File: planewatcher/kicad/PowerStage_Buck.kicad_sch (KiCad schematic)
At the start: 19 parts, among them U11 LT8640IUDCF-1#PBF

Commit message: work on board layout
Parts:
- renumbered C104 to C59, C105 to C60, C60 to C61, C61 to C62, C62 to C63, C63 to C64, C64 to C66, C66 to C67, L7 to L10, L14 to L9, R56 to R32, R26 to R33, R27 to R34, R28 to R35, TP16 to TP18, TP15 to TP19, U11 to U12
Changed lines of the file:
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@@
 		(in_pos_files yes)
 		(dnp no)
-		(property "Reference" "#PWR089"
+		(property "Reference" "#PWR097"
 			(at 161.29 81.28 0)
 			(hide yes)
@@
 			(project "planewatcher"
 				(path "/7a4a4324-e8b8-4d06-b75a-28095d4e9f10/3f548880-1f88-4cb2-a308-e70fd70c9481"
-					(reference "#PWR089")
+					(reference "#PWR097")
 					(unit 1)
 				)
@@
 		(dnp no)
 		(fields_autoplaced yes)
-		(property "Reference" "L14"
+		(property "Reference" "L9"
 			(at 99.06 54.61 90)
 			(show_name no)
@@
 			(project "planewatcher"
 				(path "/7a4a4324-e8b8-4d06-b75a-28095d4e9f10/3f548880-1f88-4cb2-a308-e70fd70c9481"
-					(reference "L14")
+					(reference "L9")
 					(unit 1)
 				)
@@
 		(dnp no)
 		(fields_autoplaced yes)
-		(property "Reference" "#PWR035"
+		(property "Reference" "#PWR099"
 			(at 119.38 107.95 0)
 			(hide yes)
@@
 			(project "planewatcher"
 				(path "/7a4a4324-e8b8-4d06-b75a-28095d4e9f10/3f548880-1f88-4cb2-a308-e70fd70c9481"
-					(reference "#PWR035")
+					(reference "#PWR099")
 					(unit 1)
 				)
@@
 		(in_pos_files yes)
 		(dnp no)
-		(property "Reference" "C63"
+		(property "Reference" "C64"
 			(at 115.57 87.63 90)
 			(show_name no)
@@
 			(project "planewatcher"
 				(path "/7a4a4324-e8b8-4d06-b75a-28095d4e9f10/3f548880-1f88-4cb2-a308-e70fd70c9481"
-					(reference "C63")
+					(reference "C64")
 					(unit 1)
 				)
@@
 		(dnp no)
 		(fields_autoplaced yes)
-		(property "Reference" "U11"
+		(property "Reference" "U12"
 			(at 143.51 110.49 0)
 			(show_name no)
@@
 			(project "planewatcher"
 				(path "/7a4a4324-e8b8-4d06-b75a-28095d4e9f10/3f548880-1f88-4cb2-a308-e70fd70c9481"
-					(reference "U11")
+					(reference "U12")
 					(unit 1)
 				)
@@
 		(in_pos_files yes)
 		(dnp no)
-		(property "Reference" "R28"
+		(property "Reference" "R35"
 			(at 119.38 117.348 90)
 			(show_name no)
@@
 			(project "planewatcher"
 				(path "/7a4a4324-e8b8-4d06-b75a-28095d4e9f10/3f548880-1f88-4cb2-a308-e70fd70c9481"
-					(reference "R28")
+					(reference "R35")
 					(unit 1)
 				)
@@
 		(dnp no)
 		(fields_autoplaced yes)
-		(property "Reference" "L7"
+		(property "Reference" "L10"
 			(at 180.34 85.09 90)
 			(show_name no)
@@
 			(project "planewatcher"
 				(path "/7a4a4324-e8b8-4d06-b75a-28095d4e9f10/3f548880-1f88-4cb2-a308-e70fd70c9481"
-					(reference "L7")
+					(reference "L10")
 					(unit 1)
 				)
@@
 		(dnp no)
 		(fields_autoplaced yes)
-		(property "Reference" "#PWR041"
+		(property "Reference" "#PWR0101"
 			(at 156.21 111.76 0)
 			(hide yes)
@@
 			(project "planewatcher"
 				(path "/7a4a4324-e8b8-4d06-b75a-28095d4e9f10/3f548880-1f88-4cb2-a308-e70fd70c9481"
-					(reference "#PWR041")
+					(reference "#PWR0101")
 					(unit 1)
 				)
@@
 		(dnp no)
 		(fields_autoplaced yes)
-		(property "Reference" "R26"
+		(property "Reference" "R33"
 			(at 193.04 96.5199 0)
 			(show_name no)
@@
 			(project "planewatcher"
 				(path "/7a4a4324-e8b8-4d06-b75a-28095d4e9f10/3f548880-1f88-4cb2-a308-e70fd70c9481"
-					(reference "R26")
+					(reference "R33")
 					(unit 1)
 				)
@@
 		(in_pos_files yes)
 		(dnp no)
-		(property "Reference" "C66"
+		(property "Reference" "C67"
 			(at 122.936 95.758 90)
 			(show_name no)
@@
 			(project "planewatcher"
 				(path "/7a4a4324-e8b8-4d06-b75a-28095d4e9f10/3f548880-1f88-4cb2-a308-e70fd70c9481"
-					(reference "C66")
+					(reference "C67")
 					(unit 1)
 				)
@@
 		(dnp no)
 		(fields_autoplaced yes)
-		(property "Reference" "C104"
+		(property "Reference" "C59"
 			(at 95.25 62.2299 0)
 			(show_name no)
@@
 			(project "planewatcher"
 				(path "/7a4a4324-e8b8-4d06-b75a-28095d4e9f10/3f548880-1f88-4cb2-a308-e70fd70c9481"
-					(reference "C104")
+					(reference "C59")
 					(unit 1)
 				)
@@
 		(in_pos_files yes)
 		(dnp no)
-		(property "Reference" "TP15"
+		(property "Reference" "TP19"
 			(at 85.344 96.012 90)
 			(show_name no)
@@
 			(project "planewatcher"
 				(path "/7a4a4324-e8b8-4d06-b75a-28095d4e9f10/3f548880-1f88-4cb2-a308-e70fd70c9481"
-					(reference "TP15")
+					(reference "TP19")
 					(unit 1)
 				)
@@
 		(in_pos_files yes)
 		(dnp no)
-		(property "Reference" "C62"
+		(property "Reference" "C63"
 			(at 164.592 85.344 0)
 			(show_name no)
@@
 			(project "planewatcher"
 				(path "/7a4a4324-e8b8-4d06-b75a-28095d4e9f10/3f548880-1f88-4cb2-a308-e70fd70c9481"
-					(reference "C62")
+					(reference "C63")
 					(unit 1)
 				)
@@
 		(dnp no)
 		(fields_autoplaced yes)
-		(property "Reference" "C60"
+		(property "Reference" "C61"
 			(at 125.73 69.8499 0)
 			(show_name no)
@@
 			(project "planewatcher"
 				(path "/7a4a4324-e8b8-4d06-b75a-28095d4e9f10/3f548880-1f88-4cb2-a308-e70fd70c9481"
-					(reference "C60")
+					(reference "C61")
 					(unit 1)
 				)
@@
 		(dnp no)
 		(fields_autoplaced yes)
-		(property "Reference" "#PWR088"
+		(property "Reference" "#PWR096"
 			(at 121.92 81.28 0)
 			(hide yes)
@@
 			(project "planewatcher"
 				(path "/7a4a4324-e8b8-4d06-b75a-28095d4e9f10/3f548880-1f88-4cb2-a308-e70fd70c9481"
-					(reference "#PWR088")
+					(reference "#PWR096")
 					(unit 1)
 				)
@@
 		(dnp no)
 		(fields_autoplaced yes)
-		(property "Reference" "R56"
+		(property "Reference" "R32"
 			(at 92.71 88.9 90)
 			(show_name no)
@@
 			(project "planewatcher"
 				(path "/7a4a4324-e8b8-4d06-b75a-28095d4e9f10/3f548880-1f88-4cb2-a308-e70fd70c9481"
-					(reference "R56")
+					(reference "R32")
 					(unit 1)
 				)
@@
 		(dnp no)
 		(fields_autoplaced yes)
-		(property "Reference" "#PWR091"
+		(property "Reference" "#PWR0100"
 			(at 204.47 107.95 0)
 			(hide yes)
@@
 			(project "planewatcher"
 				(path "/7a4a4324-e8b8-4d06-b75a-28095d4e9f10/3f548880-1f88-4cb2-a308-e70fd70c9481"
-					(reference "#PWR091")
+					(reference "#PWR0100")
 					(unit 1)
 				)
@@
 		(dnp no)
 		(fields_autoplaced yes)
-		(property "Reference" "#PWR092"
+		(property "Reference" "#PWR0102"
 			(at 190.5 115.57 0)
 			(hide yes)
@@
 			(project "planewatcher"
 				(path "/7a4a4324-e8b8-4d06-b75a-28095d4e9f10/3f548880-1f88-4cb2-a308-e70fd70c9481"
-					(reference "#PWR092")
+					(reference "#PWR0102")
 					(unit 1)
 				)
@@
 		(dnp no)
 		(fields_autoplaced yes)
-		(property "Reference" "#PWR040"
+		(property "Reference" "#PWR0103"
 			(at 114.3 128.27 0)
 			(hide yes)
@@
 			(project "planewatcher"
 				(path "/7a4a4324-e8b8-4d06-b75a-28095d4e9f10/3f548880-1f88-4cb2-a308-e70fd70c9481"
-					(reference "#PWR040")
+					(reference "#PWR0103")
 					(unit 1)
 				)
@@
 		(dnp no)
 		(fields_autoplaced yes)
-		(property "Reference" "#PWR0148"
+		(property "Reference" "#PWR095"
 			(at 106.68 73.66 0)
 			(hide yes)
@@
 			(project "planewatcher"
 				(path "/7a4a4324-e8b8-4d06-b75a-28095d4e9f10/3f548880-1f88-4cb2-a308-e70fd70c9481"
-					(reference "#PWR0148")
+					(reference "#PWR095")
 					(unit 1)
 				)
@@
 		(in_pos_files yes)
 		(dnp no)
-		(property "Reference" "TP16"
+		(property "Reference" "TP18"
 			(at 189.738 82.296 0)
 			(show_name no)
@@
 			(project "planewatcher"
 				(path "/7a4a4324-e8b8-4d06-b75a-28095d4e9f10/3f548880-1f88-4cb2-a308-e70fd70c9481"
-					(reference "TP16")
+					(reference "TP18")
 					(unit 1)
 				)
@@
 		(dnp no)
 		(fields_autoplaced yes)
-		(property "Reference" "#PWR034"
+		(property "Reference" "#PWR098"
 			(at 111.76 100.33 0)
 			(hide yes)
@@
 			(project "planewatcher"
 				(path "/7a4a4324-e8b8-4d06-b75a-28095d4e9f10/3f548880-1f88-4cb2-a308-e70fd70c9481"
-					(reference "#PWR034")
+					(reference "#PWR098")
 					(unit 1)
 				)
@@
 		(dnp no)
 		(fields_autoplaced yes)
-		(property "Reference" "#PWR0132"
+		(property "Reference" "#PWR094"
 			(at 91.44 73.66 0)
 			(hide yes)
@@
 			(project "planewatcher"
 				(path "/7a4a4324-e8b8-4d06-b75a-28095d4e9f10/3f548880-1f88-4cb2-a308-e70fd70c9481"
-					(reference "#PWR0132")
+					(reference "#PWR094")
 					(unit 1)
 				)
@@
 		(dnp no)
 		(fields_autoplaced yes)
-		(property "Reference" "C105"
+		(property "Reference" "C60"
 			(at 110.49 62.2299 0)
 			(show_name no)
@@
 			(project "planewatcher"
 				(path "/7a4a4324-e8b8-4d06-b75a-28095d4e9f10/3f548880-1f88-4cb2-a308-e70fd70c9481"
-					(reference "C105")
+					(reference "C60")
 					(unit 1)
 				)
@@
 		(dnp no)
 		(fields_autoplaced yes)
-		(property "Reference" "R27"
+		(property "Reference" "R34"
 			(at 193.04 104.1399 0)
 			(show_name no)
@@
 			(project "planewatcher"
 				(path "/7a4a4324-e8b8-4d06-b75a-28095d4e9f10/3f548880-1f88-4cb2-a308-e70fd70c9481"
-					(reference "R27")
+					(reference "R34")
 					(unit 1)
 				)
@@
 		(dnp no)
 		(fields_autoplaced yes)
-		(property "Reference" "C61"
+		(property "Reference" "C62"
 			(at 165.1 69.8499 0)
 			(show_name no)
@@
 			(project "planewatcher"
 				(path "/7a4a4324-e8b8-4d06-b75a-28095d4e9f10/3f548880-1f88-4cb2-a308-e70fd70c9481"
-					(reference "C61")
+					(reference "C62")
 					(unit 1)
 				)
@@
 		(dnp no)
 		(fields_autoplaced yes)
-		(property "Reference" "C64"
+		(property "Reference" "C66"
 			(at 208.28 96.5199 0)
 			(show_name no)
@@
 			(project "planewatcher"
 				(path "/7a4a4324-e8b8-4d06-b75a-28095d4e9f10/3f548880-1f88-4cb2-a308-e70fd70c9481"
-					(reference "C64")
-					(unit 1)
-				)
+					(reference "C66")
+					(unit 1)
+				)

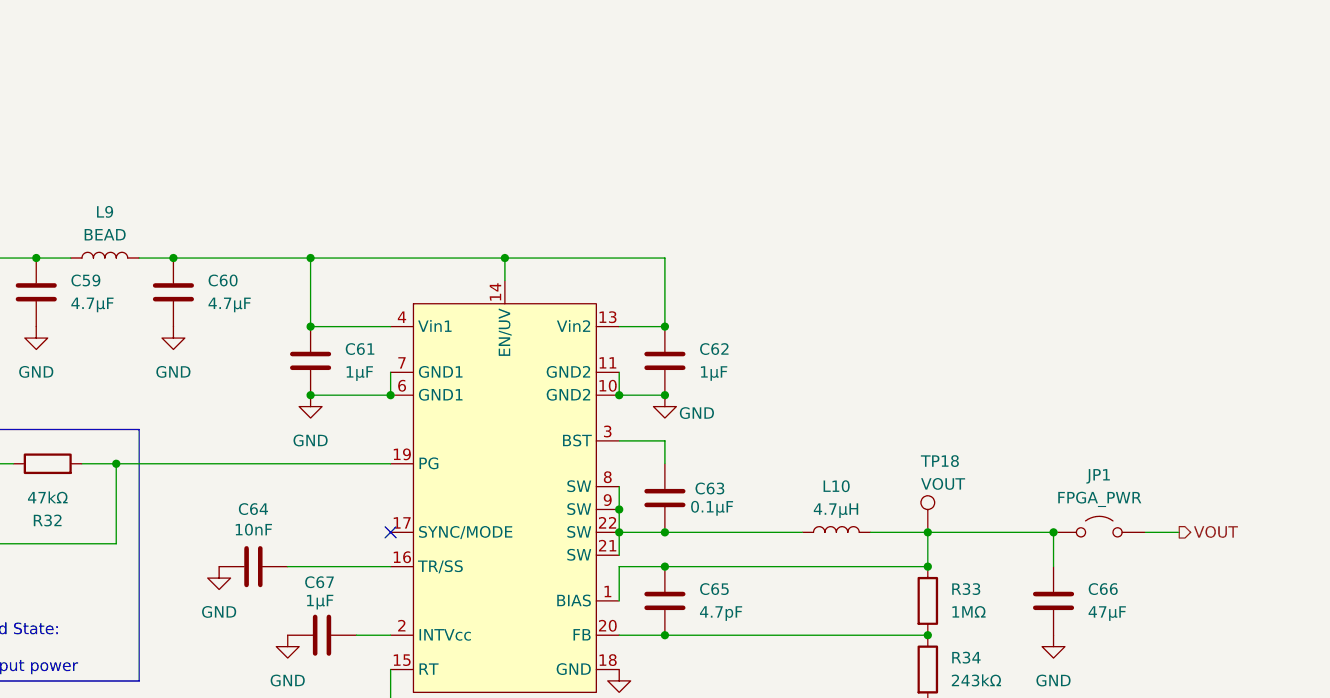
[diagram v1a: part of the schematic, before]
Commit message: address & fix ERC errors/warnings
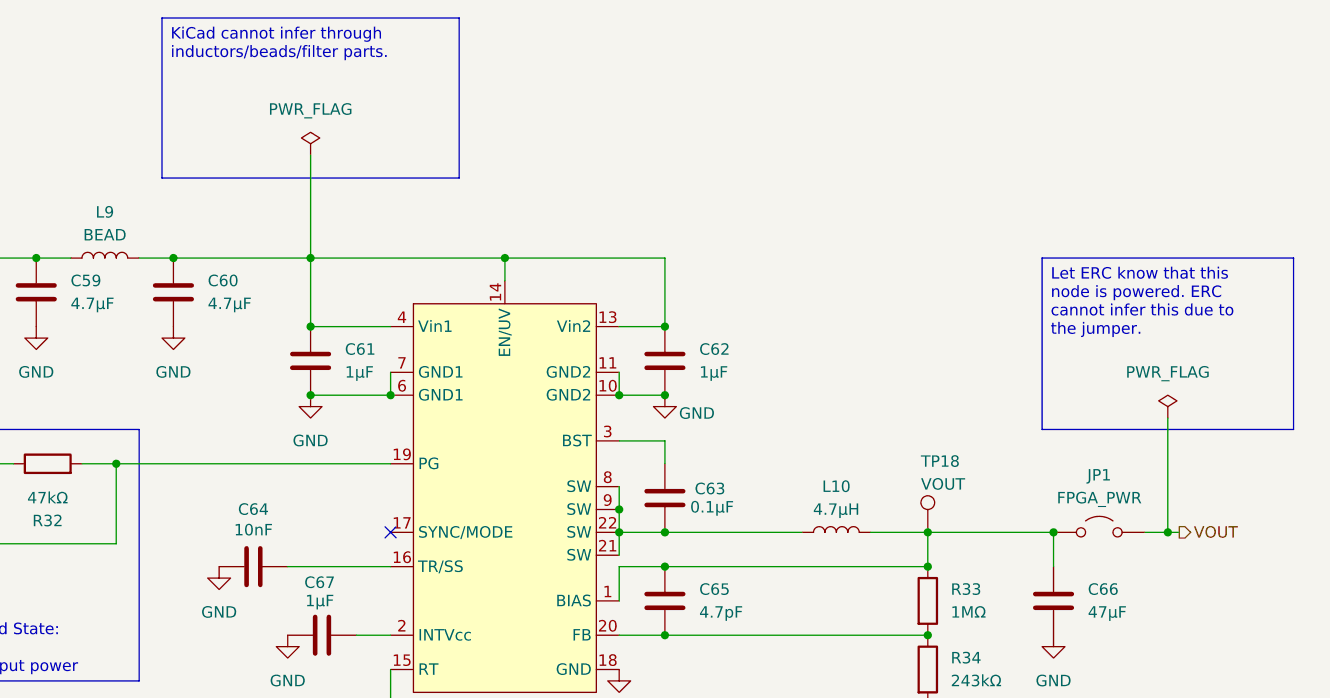
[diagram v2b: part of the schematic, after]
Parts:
- JP1: Notes (none) -> Allow FPGA power to be disconnected, if FPGA powered extern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
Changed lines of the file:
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@@
 		)
 	)
+	(text_box "Let ERC know that this node is powered. ERC cannot infer this due to the jumper."
+		(exclude_from_sim no)
+		(at 203.2 59.69 0)
+		(size 27.94 19.05)
+		(margins 0.9525 0.9525 0.9525 0.9525)
+		(stroke
+			(width 0)
+			(type solid)
+		)
+		(fill
+			(type none)
+		)
+		(effects
+			(font
+				(size 1.27 1.27)
+			)
+			(justify left top)
+		)
+	)
 	(text_box "Set switching freq. to 700kHz."
 		(exclude_from_sim no)
@@
 		)
 	)
+	(text_box "KiCad cannot infer through inductors/beads/filter parts."
+		(exclude_from_sim no)
+		(at 105.41 33.02 0)
+		(size 33.02 17.78)
+		(margins 0.9525 0.9525 0.9525 0.9525)
+		(stroke
+			(width 0)
+			(type solid)
+		)
+		(fill
+			(type none)
+		)
+		(effects
+			(font
+				(size 1.27 1.27)
+			)
+			(justify left top)
+		)
+	)
 	(junction
 		(at 190.5 93.98)
@@
 	)
 	(junction
+		(at 217.17 90.17)
+		(diameter 0)
+		(color 0 0 0 0)
+	)
+	(junction
 		(at 156.21 90.17)
 		(diameter 0)
@@
 	(wire
 		(pts
+			(xy 121.92 48.26) (xy 121.92 59.69)
+		)
+		(stroke
+			(width 0)
+			(type default)
+		)
+	)
+	(wire
+		(pts
 			(xy 119.38 93.98) (xy 130.81 93.98)
 		)
@@
 	(wire
 		(pts
+			(xy 217.17 77.47) (xy 217.17 90.17)
+		)
+		(stroke
+			(width 0)
+			(type default)
+		)
+	)
+	(wire
+		(pts
 			(xy 156.21 85.09) (xy 156.21 87.63)
 		)
@@
 	(wire
 		(pts
-			(xy 214.63 90.17) (xy 218.44 90.17)
+			(xy 214.63 90.17) (xy 217.17 90.17)
 		)
 		(stroke
@@
 	(wire
 		(pts
+			(xy 217.17 90.17) (xy 218.44 90.17)
+		)
+		(stroke
+			(width 0)
+			(type default)
+		)
+	)
+	(wire
+		(pts
 			(xy 121.92 74.93) (xy 130.81 74.93)
 		)
@@
 	)
 	(symbol
+		(lib_id "power:PWR_FLAG")
+		(at 217.17 77.47 0)
+		(unit 1)
+		(body_style 1)
+		(exclude_from_sim no)
+		(in_bom yes)
+		(on_board yes)
+		(in_pos_files yes)
+		(dnp no)
+		(fields_autoplaced yes)
+		(property "Reference" "#FLG01"
+			(at 217.17 75.565 0)
+			(hide yes)
+			(show_name no)
+			(do_not_autoplace no)
+			(effects
+				(font
+					(size 1.27 1.27)
+				)
+			)
+		)
+		(property "Value" "PWR_FLAG"
+			(at 217.17 72.39 0)
+			(show_name no)
+			(do_not_autoplace no)
+			(effects
+				(font
+					(size 1.27 1.27)
+				)
+			)
+		)
+		(property "Footprint" ""
+			(at 217.17 77.47 0)
+			(hide yes)
+			(show_name no)
+			(do_not_autoplace no)
+			(effects
+				(font
+					(size 1.27 1.27)
+				)
+			)
+		)
+		(property "Datasheet" ""
+			(at 217.17 77.47 0)
+			(hide yes)
+			(show_name no)
+			(do_not_autoplace no)
+			(effects
+				(font
+					(size 1.27 1.27)
+				)
+			)
+		)
+		(property "Description" "Special symbol for telling ERC where power comes from"
+			(at 217.17 77.47 0)
+			(hide yes)
+			(show_name no)
+			(do_not_autoplace no)
+			(effects
+				(font
+					(size 1.27 1.27)
+				)
+			)
+		)
+		(pin "1"
+		)
+		(instances
+			(project "planewatcher"
+				(path "/7a4a4324-e8b8-4d06-b75a-28095d4e9f10/3f548880-1f88-4cb2-a308-e70fd70c9481"
+					(reference "#FLG01")
+					(unit 1)
+				)
+			)
+		)
+	)
+	(symbol
 		(lib_id "power:GND")
 		(at 121.92 74.93 0)
@@
 			)
 		)
-		(property "Notes" ""
+		(property "Notes" "Allow FPGA power to be disconnected, if FPGA powered externally."
 			(at 209.55 90.17 0)
 			(hide yes)
@@
 					(unit 1)
 				)
+			)
+		)
+	)
+	(symbol
+		(lib_id "power:PWR_FLAG")
+		(at 121.92 48.26 0)
+		(unit 1)
+		(body_style 1)
+		(exclude_from_sim no)
+		(in_bom yes)
+		(on_board yes)
+		(in_pos_files yes)
+		(dnp no)
+		(fields_autoplaced yes)
+		(property "Reference" "#FLG010"
+			(at 121.92 46.355 0)
+			(hide yes)
+			(show_name no)
+			(do_not_autoplace no)
+			(effects
+				(font
+					(size 1.27 1.27)
+				)
+			)
+		)
+		(property "Value" "PWR_FLAG"
+			(at 121.92 43.18 0)
+			(show_name no)
+			(do_not_autoplace no)
+			(effects
+				(font
+					(size 1.27 1.27)
+				)
+			)
+		)
+		(property "Footprint" ""
+			(at 121.92 48.26 0)
+			(hide yes)
+			(show_name no)
+			(do_not_autoplace no)
+			(effects
+				(font
+					(size 1.27 1.27)
+				)
+			)
+		)
+		(property "Datasheet" ""
+			(at 121.92 48.26 0)
+			(hide yes)
+			(show_name no)
+			(do_not_autoplace no)
+			(effects
+				(font
+					(size 1.27 1.27)
+				)
+			)
+		)
+		(property "Description" "Special symbol for telling ERC where power comes from"
+			(at 121.92 48.26 0)
+			(hide yes)
+			(show_name no)
+			(do_not_autoplace no)
+			(effects
+				(font
+					(size 1.27 1.27)
+				)
+			)
+		)
+		(pin "1"
+		)
+		(instances
+			(project "planewatcher"
+				(path "/7a4a4324-e8b8-4d06-b75a-28095d4e9f10/3f548880-1f88-4cb2-a308-e70fd70c9481"
+					(reference "#FLG010")
+					(unit 1)
+				)

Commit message: updates before fab
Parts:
- C59, C60: Purpose (none) -> Input ceramic capacitor for the LT8640 buck regulator.; Suggested Part (none) -> Murata GRM31CR71E475KA88L
- C61, C62: Purpose (none) -> Local 1µF VIN bypass capacitor for the LT8640 buck regulato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; Suggested Part (none) -> Murata GRM188R61C105KA93D
- C63: Purpose (none) -> LT8640 BST-to-SW bootstrap capacitor for the high-side swit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; Suggested Part (none) -> Murata GRM155R71H104KE14D
- C64: Purpose (none) -> Soft-start or regulator control bypass capacitor in the LT8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; Suggested Part (none) -> Murata GRM155R71H103KA88D
- C65: Purpose (none) -> Feed-forward/compensation capacitor across the LT8640 feedb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; Suggested Part (none) -> Murata GRM1555C1H4R7CA01D
- C66: Purpose (none) -> LT8640 output bulk capacitor for FPGA rail ripple and load 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; Suggested Part (none) -> KEMET C1210C476M4PACTU
- C67: Purpose (none) -> Regulator auxiliary/input bypass capacitor in the LT8640 bu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; Suggested Part (none) -> Murata GRM155R61C105KA12D
- JP1: Purpose (none) -> Allows the FPGA power rail to be linked or isolated during 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; Suggested Part (none) -> Samtec TSW-102-07-L-S
- L10: Purpose (none) -> LT8640 buck switching inductor for the FPGA 5V supply.; Suggested Part (none) -> Coilcraft XAL5030-472ME
- L9: Purpose (none) -> Filters high-frequency switching noise on the LT8640 regula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; Suggested Part (none) -> Murata BLM21PG600SN1D
- R32: Purpose (none) -> LT8640 power-good pull-up or regulator status bias resistor.; Suggested Part (none) -> Yageo RC0402FR-0747KL
- R33: Purpose (none) -> Top feedback resistor setting the LT8640 FPGA 5V output vol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; Suggested Part (none) -> Yageo RC0402FR-071ML
- R34: Purpose (none) -> Bottom/trim feedback resistor setting the LT8640 output vol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; Suggested Part (none) -> Yageo RC0402FR-07243KL
- R35: Purpose (none) -> LT8640 RT resistor setting the FPGA buck switching frequenc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; Suggested Part (none) -> Yageo RC0402FR-0760K4L
- TP18: Purpose (none) -> Provides oscilloscope/DMM probe access to VOUT.; Suggested Part (none) -> No fitted part (PCB pad only); now left out of the parts list
- TP19: Purpose (none) -> Provides oscilloscope/DMM probe access to PG.; Suggested Part (none) -> No fitted part (PCB pad only); now left out of the parts list
- U12: Purpose (none) -> Generates the FPGA 5V rail from the protected input supply.; Suggested Part (none) -> Analog Devices LT8640IUDCF-1#PBF

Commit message: updates before fab
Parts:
- JP1: now not fitted
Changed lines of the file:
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@@
 		(on_board yes)
 		(in_pos_files yes)
-		(dnp no)
+		(dnp yes)
 		(fields_autoplaced yes)
 		(property "Reference" "JP1"

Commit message: rationalise power to single 3V3 rail fed from FPGA VCC
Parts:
- U12: now not fitted
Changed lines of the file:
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@@
 		(on_board yes)
 		(in_pos_files yes)
-		(dnp no)
+		(dnp yes)
 		(fields_autoplaced yes)
 		(property "Reference" "U12"

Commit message: Add persistent PCBWay BOM fields to KiCad schematic
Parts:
- C59, C60: MPN (none) -> GRM31CR71E475KA88L; Manufacturer (none) -> Murata; Package (none) -> 1206
- C61, C62: MPN (none) -> GRM188R61C105KA93D; Manufacturer (none) -> Murata; Package (none) -> 0603
- C63: MPN (none) -> GRM155R71H104KE14D; Manufacturer (none) -> Murata; Package (none) -> 0402
- C64: MPN (none) -> GRM155R71H103KA88D; Manufacturer (none) -> Murata; Package (none) -> 0402
- C65: MPN (none) -> GRM1555C1H4R7CA01D; Manufacturer (none) -> Murata; Package (none) -> 0402
- C66: MPN (none) -> C1210C476M4PACTU; Manufacturer (none) -> KEMET; Package (none) -> 1210
- C67: MPN (none) -> GRM155R61C105KA12D; Manufacturer (none) -> Murata; Package (none) -> 0402
- JP1: MPN (none) -> TSW-102-07-L-S; Manufacturer (none) -> Samtec; Package (none) -> Pin header 1x2 2.54mm
- L10: MPN (none) -> XAL5030-472ME; Manufacturer (none) -> Coilcraft; Package (none) -> XAL5030 (5x5mm)
- L9: MPN (none) -> BLM21PG600SN1D; Manufacturer (none) -> Murata; Package (none) -> 0805
- R32: MPN (none) -> RC0402FR-0747KL; Manufacturer (none) -> Yageo; Package (none) -> 0402
- R33: MPN (none) -> RC0402FR-071ML; Manufacturer (none) -> Yageo; Package (none) -> 0402
- R34: MPN (none) -> RC0402FR-07243KL; Manufacturer (none) -> Yageo; Package (none) -> 0402
- R35: MPN (none) -> RC0402FR-0760K4L; Manufacturer (none) -> Yageo; Package (none) -> 0402
- U12: MPN (none) -> LT8640IUDCF-1#PBF; Manufacturer (none) -> Analog Devices; Package (none) -> QFN-18 (3x4mm)
